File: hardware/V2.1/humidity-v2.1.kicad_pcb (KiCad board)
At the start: 2 copper layers, 30 x 25 mm, 24 parts, among them P101 CON-SENSOR2, P102 DEBUG, P103 BOOT, U101 XMC1100-16, U102 HDC1080, U103 DRILL, U104 DRILL, U105 DRILL, U106 DRILL

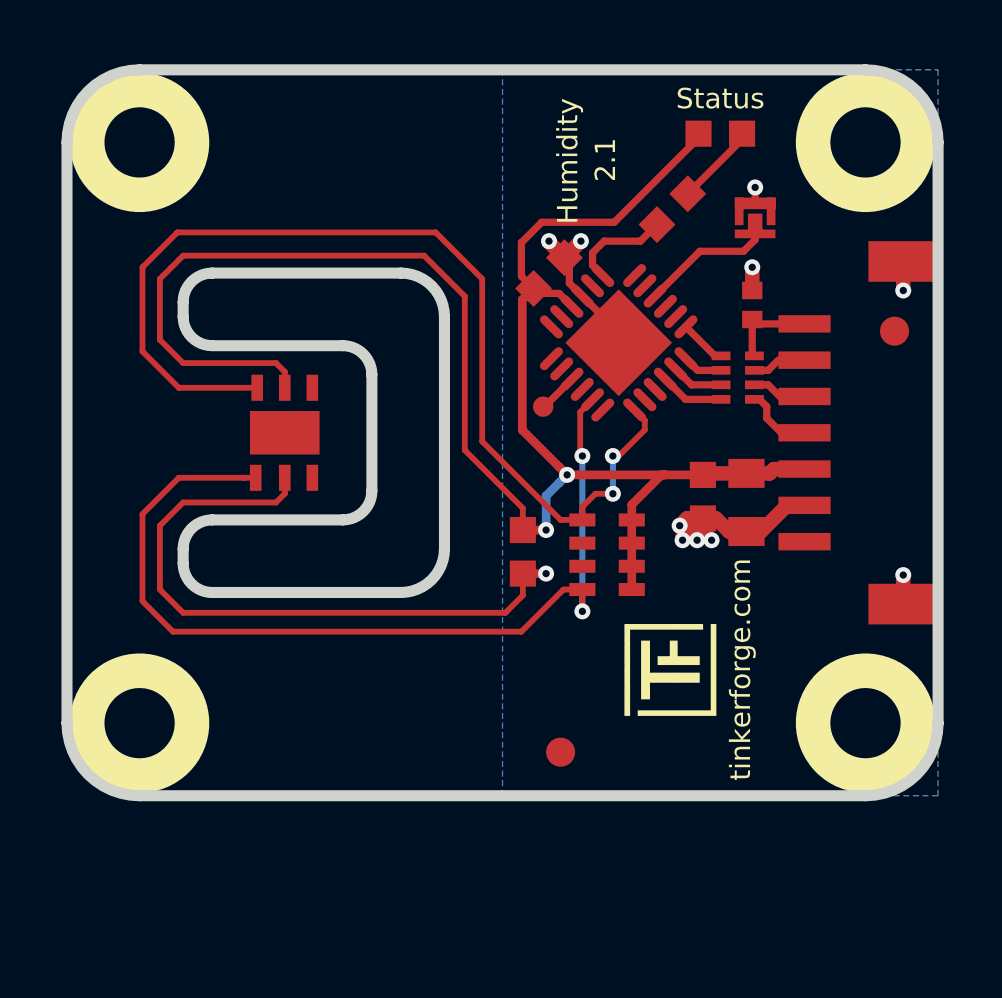
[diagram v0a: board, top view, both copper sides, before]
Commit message: new inverted slot design
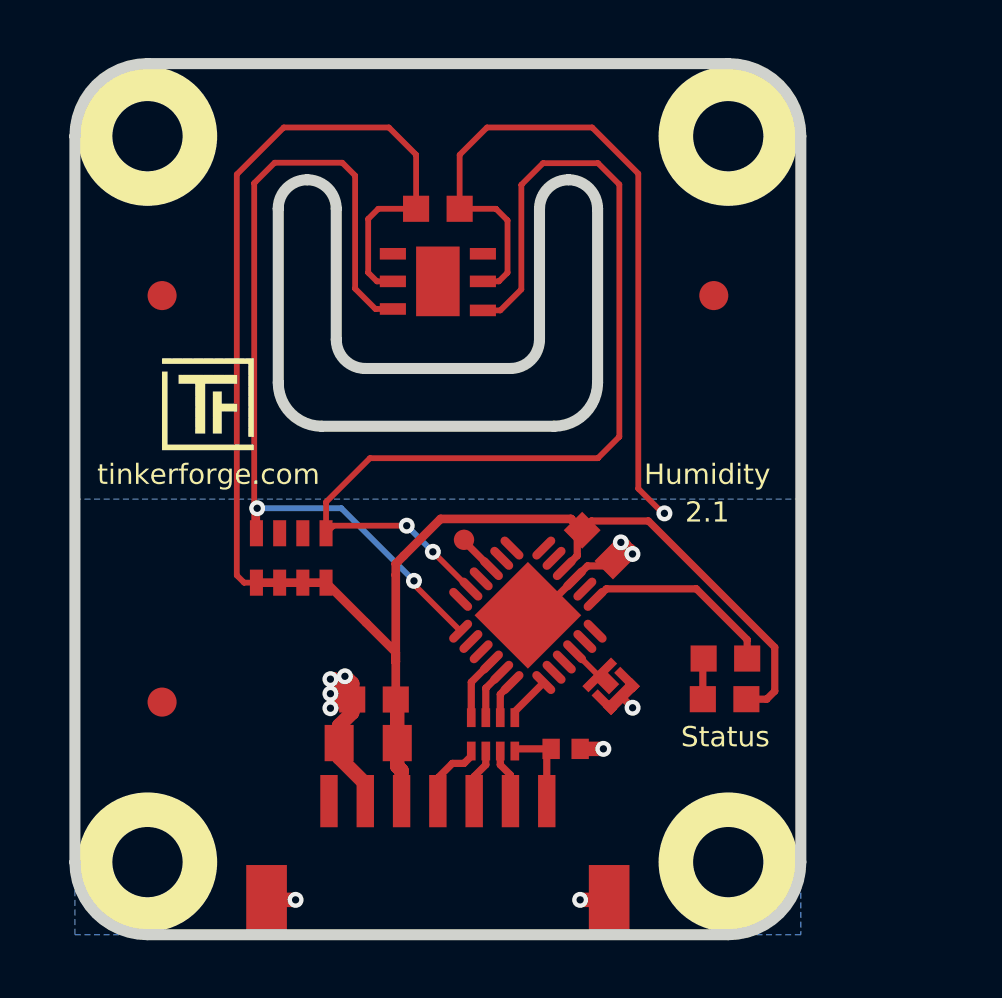
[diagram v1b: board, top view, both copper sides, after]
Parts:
- added Fiducial_Mark: VAL**, kicad-libraries:Fiducial_Mark, F.Cu at (128.4, 136.3)
- moved U103 25.2 mm to (147.9, 155.8), turned to 270 degrees
- moved U104 25.2 mm to (127.9, 155.8), turned to 270 degrees
- moved P101 24.4 mm to (137.9, 158.3), turned to 0 degrees
- moved U105 20.3 mm to (147.9, 130.8), turned to 270 degrees
- moved U106 20.2 mm to (127.9, 130.8), turned to 270 degrees
- moved G*** 20.1 mm to (128.4, 138.4), turned to 0 degrees
- moved D101 19.5 mm to (147.7, 150.2), turned to 180 degrees
- moved G*** 17.0 mm to (137.8, 149.5), turned to 180 degrees
- moved P103 16.9 mm to (143.8, 149.7), turned to 135 degrees
- moved C102 16.6 mm to (142.3, 151.9), turned to 180 degrees
- moved VAL 15.9 mm to (131.9, 149.5), turned to 180 degrees
- moved R101 15.6 mm to (147.8, 148.8), turned to 180 degrees
- moved C101 15.4 mm to (135.5, 151.7), turned to 0 degrees
- moved RP101 14.9 mm to (139.8, 151.4), turned to 0 degrees
- moved Fiducial_Mark 13.8 mm to (128.4, 150.3), turned to 270 degrees
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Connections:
- RP102 pad 5: SCL -> SDA
- RP102 pad 8: SDA -> SCL
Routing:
- net SCL: track 35.7 -> 31.2 mm
- net SDA: track 31.8 -> 36.0 mm
- net Net-(R101-Pad1): track 3.55 -> 6.76 mm
- net GND: track 43.5 -> 46.7 mm
- net Net-(P103-Pad2): track 4.85 -> 2.00 mm
- net Net-(D101-Pad2): track 3.03 -> 1.48 mm
- net VCC: track 61.8 -> 62.6 mm, vias 2 -> 0
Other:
- board size 30 x 25 mm -> 25 x 30 mm
- net class Default: clearance 0.15 -> 0.149
- rule trace_clearance: 0.15 -> 0.149
